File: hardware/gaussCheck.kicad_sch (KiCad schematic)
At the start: 3 parts, among them U1 TLV493D, U2 VIM-878-DP

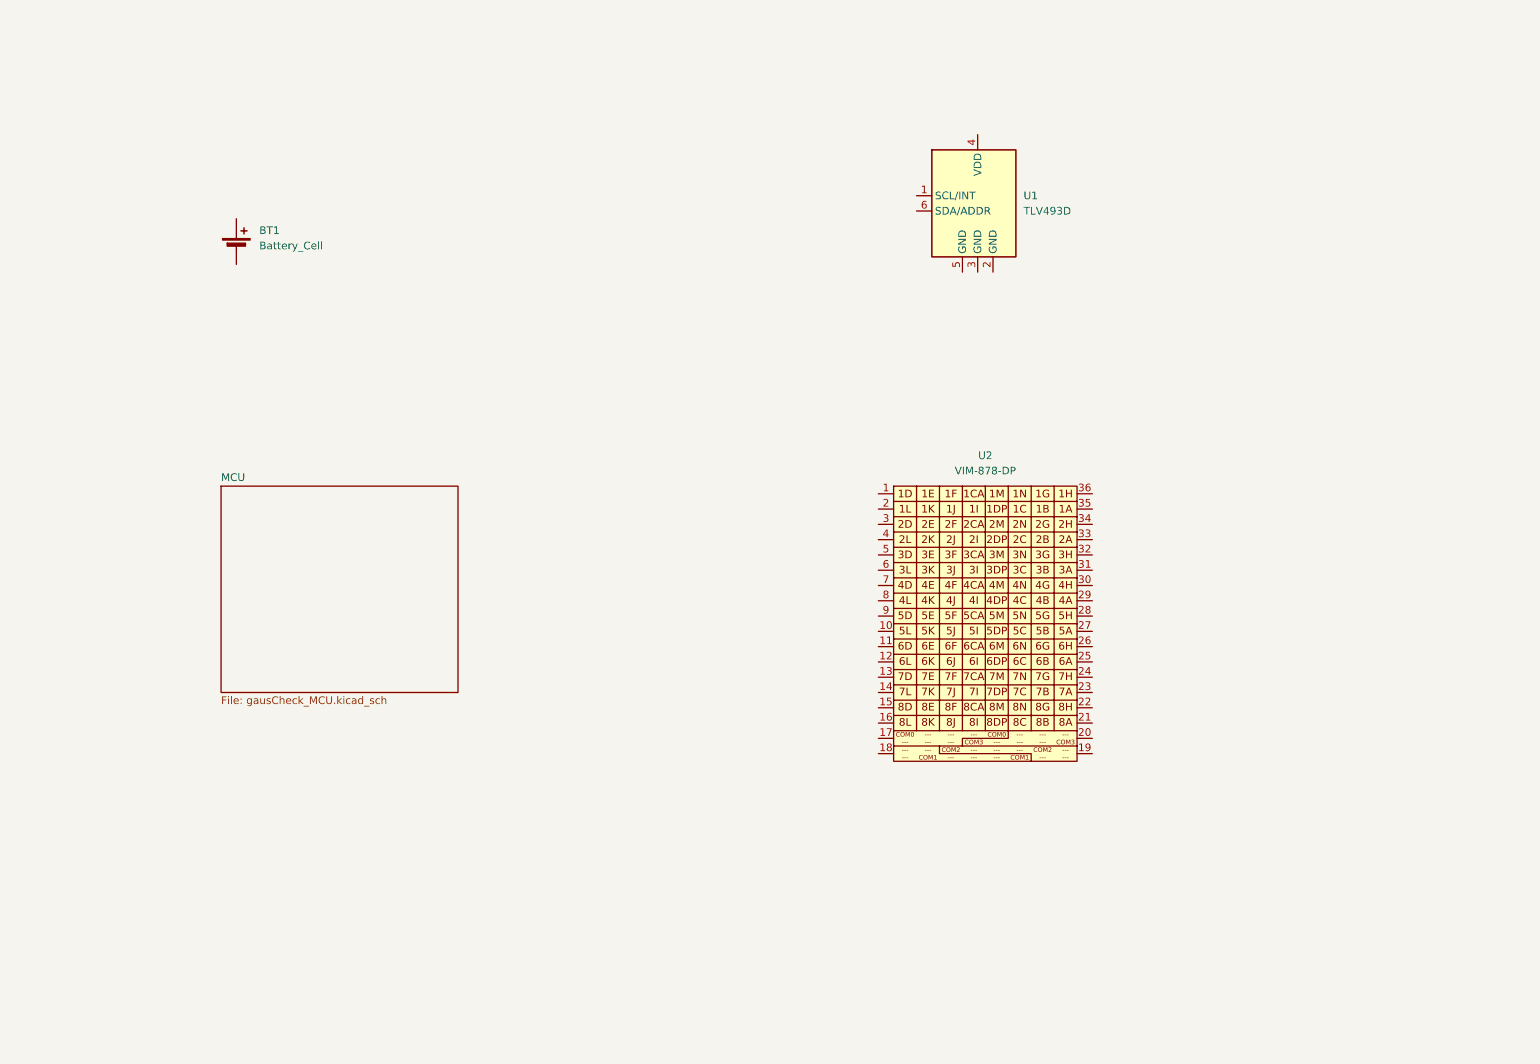
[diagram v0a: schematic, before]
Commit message: SCH - display lines
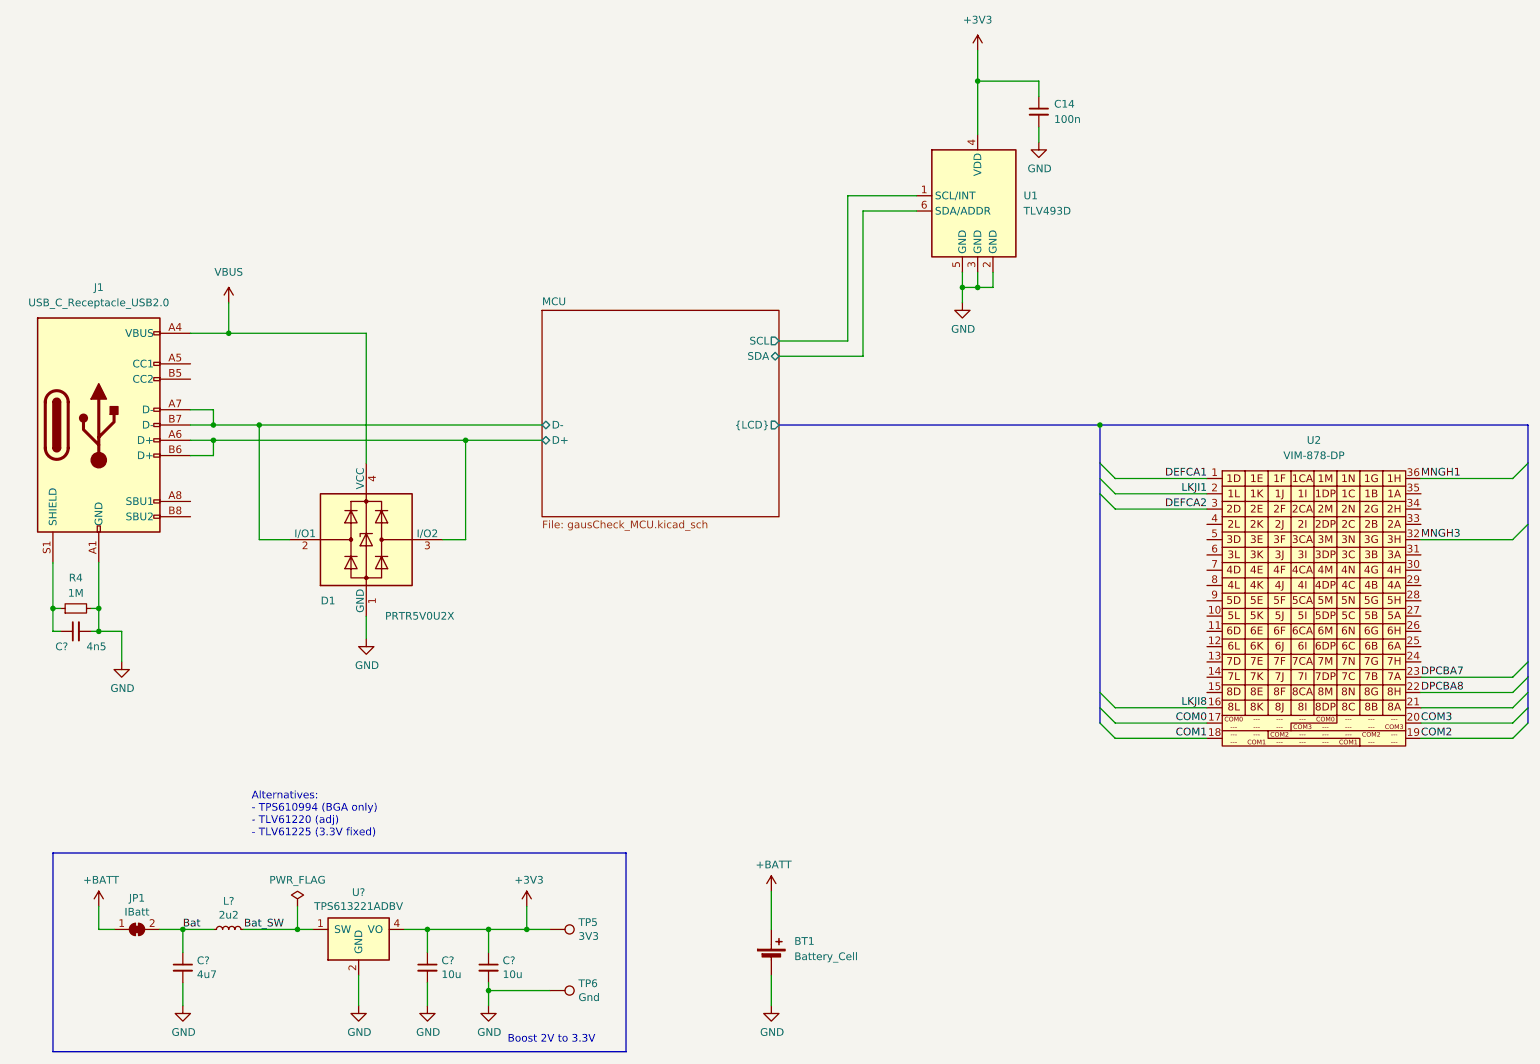
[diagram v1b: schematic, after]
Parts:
- added C14: 100n, symbol Device:C_Small
- added C?: 4u7, Capacitor_SMD:C_0603_1608Metric, symbol Device:C_Small
- added C? (x2): 10u, Capacitor_SMD:C_0603_1608Metric, symbol Device:C_Small
- added C?: 4n5, Capacitor_SMD:C_0603_1608Metric, symbol Device:C_Small
- added D1: PRTR5V0U2X, Package_TO_SOT_SMD:SOT-143, symbol Power_Protection:PRTR5V0U2X
- added J1: USB_C_Receptacle_USB2.0, Connector_USB:USB_C_Receptacle_JAE_DX07S016JA1R1500, symbol Connector:USB_C_Receptacle_USB2.0
- added JP1: IBatt, Jumper:SolderJumper-2_P1.3mm_Bridged_Pad1.0x1.5mm, symbol Jumper:SolderJumper_2_Bridged
- added L?: 2u2, Knochi_Inductors:L_Murata_0806_2.00x1.60mm, symbol Device:L_Small
- added R4: 1M, symbol Device:R_Small
- added TP5: 3V3, TestPoint:TestPoint_Pad_D1.5mm, symbol Connector:TestPoint
- added TP6: Gnd, TestPoint:TestPoint_Pad_D1.5mm, symbol Connector:TestPoint
- added U?: TPS613221ADBV, Package_TO_SOT_SMD:SOT-23-5, symbol SaniRemote-rescue:TPS613221ADBV-Knochi_Analog
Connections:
- net DEFCA1: now reaches U2.1 (1DEFCA)
- net LKJI8: now reaches U2.16 (8LKJI)
- net COM0: now reaches U2.17 (COM0)
- net COM1: now reaches U2.18 (COM1)
- net COM2: now reaches U2.19 (COM2)
- net LKJI1: now reaches U2.2 (1LKJI)
- net COM3: now reaches U2.20 (COM3)
- net DPCBA8: now reaches U2.22 (8MNGH)
- net DPCBA7: now reaches U2.23 (7DPCBA)
- net DEFCA2: now reaches U2.3 (2DEFCA)
- net MNGH3: now reaches U2.32 (8MNGH)
- net MNGH1: now reaches U2.36 (1MNGH)
- net MCU/SCL: now reaches U1.1 (SCL/INT)
- net GND: now reaches U1.2 (GND)
- net GND: now also BT1.2 (-), U1.3 (GND), U1.5 (GND), C14.2, C?.2, C?.2, C?.2, C?.2, D1.1 (GND), J1.A1 (GND), J1.A12 (GND), J1.B1 (GND), J1.B12 (GND), R4.2, TP6.1, U?.2 (GND)
- net +3V3: now reaches U1.4 (VDD)
- net +3V3: now also C14.1, C?.1, C?.1, TP5.1, U?.4 (VO)
- net MCU/SDA: now reaches U1.6 (SDA/ADDR)
- net +BATT: now reaches BT1.1 (+)
- net +BATT: now also JP1.1 (A)
- new net: C?.1, J1.S1 (SHIELD), R4.1
- new net Bat: C?.1, JP1.2 (B), L?.1
- new net Bat_SW: L?.2, U?.1 (SW)
- new net MCU/D+: D1.3 (I/O2), J1.A6 (D+), J1.B6 (D+)
- new net MCU/D-: D1.2 (I/O1), J1.A7 (D-), J1.B7 (D-)
- new net VBUS: D1.4 (VCC), J1.A4 (VBUS), J1.A9 (VBUS), J1.B4 (VBUS), J1.B9 (VBUS)
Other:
- sheet MCU ports: added D+, D-, SCL, SDA, {LCD}; removed none
- note added: "Alternatives: - TPS610994 (BGA only) - TLV61220 (adj) - TLV61225 (3.3V fixed)"
- note added: "Boost 2V to 3.3V"
- moved on the sheet: BT1, U2

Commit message: more schematic work, added buttons and led lcd wiring done
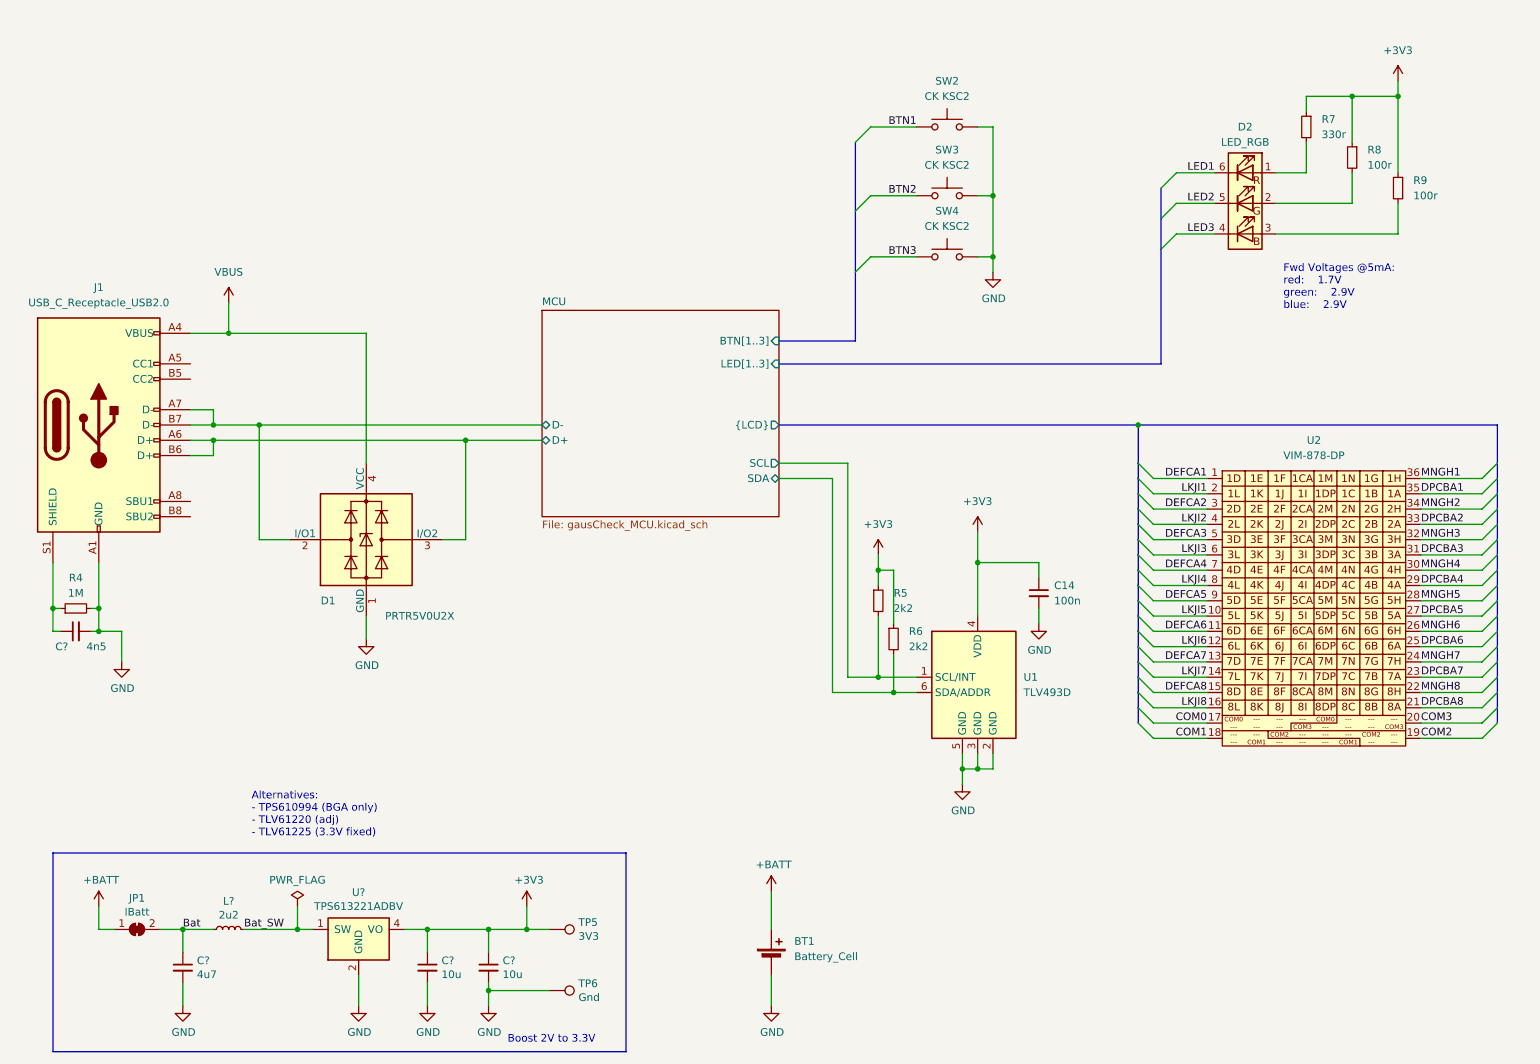
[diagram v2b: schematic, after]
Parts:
- added D2: LED_RGB, LED_SMD:LED_RGB_Cree-PLCC-6_6x5mm_P2.1mm, symbol GaussCheckCustomSymbols:LED_3A_RGB_3C
- added R5, R6: 2k2, Resistor_SMD:R_0603_1608Metric, symbol Device:R_Small
- added R7: 330r, Resistor_SMD:R_0603_1608Metric, symbol Device:R_Small
- added R8, R9: 100r, Resistor_SMD:R_0603_1608Metric, symbol Device:R_Small
- added SW2, SW3, SW4: CK KSC2, Button_Switch_SMD:SW_Push_1P1T_NO_CK_KSC7xxJ, symbol Switch:SW_Push
- BT1: footprint Battery:BatteryHolder_Keystone_3002_1x2032 -> Battery:BatteryHolder_Keystone_3034_1x20mm
- C14: footprint (none) -> Capacitor_SMD:C_0603_1608Metric
- R4: footprint (none) -> Resistor_SMD:R_0603_1608Metric
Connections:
- net +3V3: now also R5.1, R6.1, R7.1, R8.1, R9.1
- net DPCBA8: now also U2.21 (8DPCBA); no longer U2.22 (8MNGH)
- net GND: now also SW2.2, SW3.2, SW4.2
- net MCU/SCL: now also R5.2
- net MCU/SDA: now also R6.2
- net LKJI5: now reaches U2.10 (5LKJI)
- net DEFCA6: now reaches U2.11 (6DEFCA)
- net LKJI6: now reaches U2.12 (6LKJI)
- net DEFCA7: now reaches U2.13 (7DEFCA)
- net LKJI7: now reaches U2.14 (7LKJI)
- net DEFCA8: now reaches U2.15 (8DEFCA)
- net MNGH7: now reaches U2.24 (7MNGH)
- net DPCBA6: now reaches U2.25 (6DPCBA)
- net MNGH6: now reaches U2.26 (6MNGH)
- net DPCBA5: now reaches U2.27 (8DPCBA)
- net MNGH5: now reaches U2.28 (8MNGH)
- net DPCBA4: now reaches U2.29 (8DPCBA)
- net MNGH4: now reaches U2.30 (8MNGH)
- net DPCBA3: now reaches U2.31 (8DPCBA)
- net DPCBA2: now reaches U2.33 (8DPCBA)
- net MNGH2: now reaches U2.34 (8MNGH)
- net DPCBA1: now reaches U2.35 (1DPCBA)
- net LKJI2: now reaches U2.4 (2LKJI)
- net DEFCA3: now reaches U2.5 (3DEFCA)
- net LKJI3: now reaches U2.6 (3LKJI)
- net DEFCA4: now reaches U2.7 (4DEFCA)
- net LKJI4: now reaches U2.8 (4LKJI)
- net DEFCA5: now reaches U2.9 (5DEFCA)
- new net: D2.2 (GK), R8.2
- new net: D2.3 (BK), R9.2
- new net: D2.1 (RK), R7.2
- new net BTN1: SW2.1
- new net BTN2: SW3.1
- new net BTN3: SW4.1
- new net LED1: D2.6 (RA)
- new net LED2: D2.5 (GA)
- new net LED3: D2.4 (BA)
- new net MNGH8: U2.22 (8MNGH)
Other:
- sheet MCU ports: added BTN[1..3], LED[1..3]; removed none
- note added: "Fwd Voltages @5mA: red: 1.7V green: 2.9V blue: 2.9V"
- moved on the sheet: C14, U1

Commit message: added 3Dmodel for Display centered and locked key components
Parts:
- U2: MPN (none) -> VIM-878-DP-FC-S-LV
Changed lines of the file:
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@@
+      (effects (font (size 1.27 1.27)) hide)
+    )
+    (property "MPN" "VIM-878-DP-FC-S-LV" (at 229.87 119.38 0)
       (effects (font (size 1.27 1.27)) hide)
     )

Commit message: added 3D models to pushbuttons
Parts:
- J1: DIGIKEY (none) -> 670-DX07S016JA1R1500CT-ND; MPN (none) -> DX07S016JA1R1500
- SW2, SW3, SW4: MPN (none) -> KSC721J LFS
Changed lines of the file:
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@@
       (effects (font (size 1.27 1.27)) hide)
     )
-    (property "Datasheet" "~" (at 168.91 34.29 0)
+    (property "Datasheet" "https://www.ckswitches.com/media/1973/ksc7.pdf" (at 168.91 34.29 0)
+      (effects (font (size 1.27 1.27)) hide)
+    )
+    (property "MPN" "KSC721J LFS" (at 168.91 39.37 0)
       (effects (font (size 1.27 1.27)) hide)
     )
@@
       (effects (font (size 1.27 1.27)) hide)
     )
+    (property "MPN" "DX07S016JA1R1500" (at 27.94 88.9 0)
+      (effects (font (size 1.27 1.27)) hide)
+    )
+    (property "DIGIKEY" "670-DX07S016JA1R1500CT-ND" (at 27.94 88.9 0)
+      (effects (font (size 1.27 1.27)) hide)
+    )
     (pin "A1")
     (pin "A12")
@@
       (effects (font (size 1.27 1.27)) hide)
     )
-    (property "Datasheet" "~" (at 168.91 45.72 0)
+    (property "Datasheet" "https://www.ckswitches.com/media/1973/ksc7.pdf" (at 168.91 45.72 0)
+      (effects (font (size 1.27 1.27)) hide)
+    )
+    (property "MPN" "KSC721J LFS" (at 168.91 50.8 0)
       (effects (font (size 1.27 1.27)) hide)
     )
@@
       (effects (font (size 1.27 1.27)) hide)
     )
-    (property "Datasheet" "~" (at 168.91 55.88 0)
-      (effects (font (size 1.27 1.27)) hide)
-    )
+    (property "Datasheet" "https://www.ckswitches.com/media/1973/ksc7.pdf" (at 168.91 55.88 0)
+      (effects (font (size 1.27 1.27)) hide)
+    )
+    (property "MPN" "KSC721J LFS" (at 168.91 60.96 0)
+      (effects (font (size 1.27 1.27)) hide)
+    )

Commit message: Turned MCU by 45degress and rerouted
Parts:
- J1: footprint Connector_USB:USB_C_Receptacle_JAE_DX07S016JA1R1500 -> Connector_USB:USB_C_Receptacle_GCT_USB4105-xx-A_16P_TopMnt_Horizontal; DIGIKEY 670-DX07S016JA1R1500CT-ND -> 2073-USB4105-GF-ACT-ND; MPN DX07S016JA1R1500 -> USB4105-GF-A
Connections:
- net Bat renamed BATT
- net Bat_SW renamed BATT_SW
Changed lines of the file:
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@@
     (effects (font (size 1.27 1.27)) (justify right bottom))
   )
-  (label "Bat_SW" (at 52.07 172.72 0) (fields_autoplaced)
+  (label "BATT_SW" (at 52.07 172.72 0) (fields_autoplaced)
     (effects (font (size 1.27 1.27)) (justify left bottom))
   )
@@
     (effects (font (size 1.27 1.27)) (justify right bottom))
   )
-  (label "Bat" (at 41.91 172.72 0) (fields_autoplaced)
+  (label "BATT" (at 41.91 172.72 0) (fields_autoplaced)
     (effects (font (size 1.27 1.27)) (justify left bottom))
   )
@@
       (effects (font (size 1.27 1.27)))
     )
-    (property "Footprint" "Connector_USB:USB_C_Receptacle_JAE_DX07S016JA1R1500" (at 31.75 88.9 0)
+    (property "Footprint" "Connector_USB:USB_C_Receptacle_GCT_USB4105-xx-A_16P_TopMnt_Horizontal" (at 31.75 88.9 0)
       (effects (font (size 1.27 1.27)) hide)
     )
@@
       (effects (font (size 1.27 1.27)) hide)
     )
-    (property "MPN" "DX07S016JA1R1500" (at 27.94 88.9 0)
-      (effects (font (size 1.27 1.27)) hide)
-    )
-    (property "DIGIKEY" "670-DX07S016JA1R1500CT-ND" (at 27.94 88.9 0)
-      (effects (font (size 1.27 1.27)) hide)
-    )
+    (property "MPN" "USB4105-GF-A" (at 27.94 88.9 0)
+      (effects (font (size 1.27 1.27)) hide)
+    )
+    (property "DIGIKEY" "2073-USB4105-GF-ACT-ND" (at 27.94 88.9 0)
+      (effects (font (size 1.27 1.27)) hide)
+    )

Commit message: minor adjustments
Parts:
- D2: MPN (none) -> CLP6C-FKB-CKNPRGJBB7a363
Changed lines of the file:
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@@
       (effects (font (size 1.27 1.27)) hide)
     )
-    (property "Datasheet" "~" (at 218.44 53.34 0)
+    (property "Datasheet" "https://www.mouser.de/datasheet/2/723/CLP6CRKWAKW-2326647.pdf" (at 218.44 53.34 0)
       (effects (font (size 1.27 1.27)) hide)
     )
+    (property "MPN" "CLP6C-FKB-CKNPRGJBB7a363" (at 218.44 52.07 0)
+      (effects (font (size 1.27 1.27)) hide)
+    )

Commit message: moved buttons to the side JTAG to the bottom reset to the bottom
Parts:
- SW2, SW3, SW4: value CK KSC2 -> PT847S; footprint Button_Switch_SMD:SW_Push_1P1T_NO_CK_KSC7xxJ -> GaussCheckCustomFootprint:SW_SPST_CK_PTS847MMxxxSMT_4.6x2.2mm; MPN KSC721J LFS -> PTS847MM350SMTR2
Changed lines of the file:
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@@
       (effects (font (size 1.27 1.27)))
     )
-    (property "Value" "CK KSC2" (at 168.91 34.29 0)
-      (effects (font (size 1.27 1.27)))
-    )
-    (property "Footprint" "Button_Switch_SMD:SW_Push_1P1T_NO_CK_KSC7xxJ" (at 168.91 34.29 0)
+    (property "Value" "PT847S" (at 168.91 34.29 0)
+      (effects (font (size 1.27 1.27)))
+    )
+    (property "Footprint" "GaussCheckCustomFootprint:SW_SPST_CK_PTS847MMxxxSMT_4.6x2.2mm" (at 168.91 34.29 0)
       (effects (font (size 1.27 1.27)) hide)
     )
@@
       (effects (font (size 1.27 1.27)) hide)
     )
-    (property "MPN" "KSC721J LFS" (at 168.91 39.37 0)
+    (property "MPN" "PTS847MM350SMTR2 " (at 168.91 39.37 0)
       (effects (font (size 1.27 1.27)) hide)
     )
@@
       (effects (font (size 1.27 1.27)))
     )
-    (property "Value" "CK KSC2" (at 168.91 45.72 0)
-      (effects (font (size 1.27 1.27)))
-    )
-    (property "Footprint" "Button_Switch_SMD:SW_Push_1P1T_NO_CK_KSC7xxJ" (at 168.91 45.72 0)
+    (property "Value" "PT847S" (at 168.91 45.72 0)
+      (effects (font (size 1.27 1.27)))
+    )
+    (property "Footprint" "GaussCheckCustomFootprint:SW_SPST_CK_PTS847MMxxxSMT_4.6x2.2mm" (at 168.91 45.72 0)
       (effects (font (size 1.27 1.27)) hide)
     )
@@
       (effects (font (size 1.27 1.27)) hide)
     )
-    (property "MPN" "KSC721J LFS" (at 168.91 50.8 0)
+    (property "MPN" "PTS847MM350SMTR2 " (at 168.91 50.8 0)
       (effects (font (size 1.27 1.27)) hide)
     )
@@
       (effects (font (size 1.27 1.27)))
     )
-    (property "Value" "CK KSC2" (at 168.91 55.88 0)
-      (effects (font (size 1.27 1.27)))
-    )
-    (property "Footprint" "Button_Switch_SMD:SW_Push_1P1T_NO_CK_KSC7xxJ" (at 168.91 55.88 0)
+    (property "Value" "PT847S" (at 168.91 55.88 0)
+      (effects (font (size 1.27 1.27)))
+    )
+    (property "Footprint" "GaussCheckCustomFootprint:SW_SPST_CK_PTS847MMxxxSMT_4.6x2.2mm" (at 168.91 55.88 0)
       (effects (font (size 1.27 1.27)) hide)
     )
@@
       (effects (font (size 1.27 1.27)) hide)
     )
-    (property "MPN" "KSC721J LFS" (at 168.91 60.96 0)
-      (effects (font (size 1.27 1.27)) hide)
-    )
+    (property "MPN" "PTS847MM350SMTR2 " (at 168.91 60.96 0)
+      (effects (font (size 1.27 1.27)) hide)
+    )
